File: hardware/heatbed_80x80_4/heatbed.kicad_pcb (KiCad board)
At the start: 2 copper layers, 80 x 80 mm, 1 part, among them J1 PWR

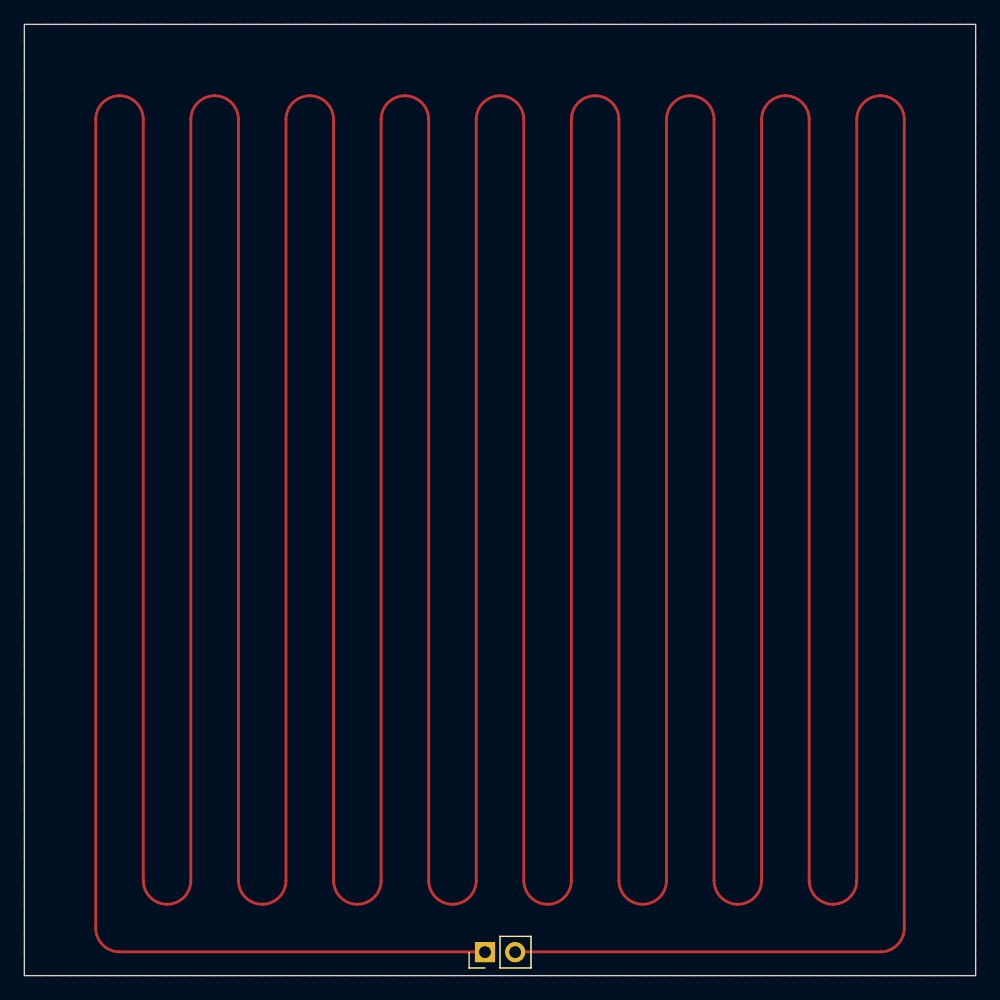
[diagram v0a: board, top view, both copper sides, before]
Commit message: Further increase tracks' widths
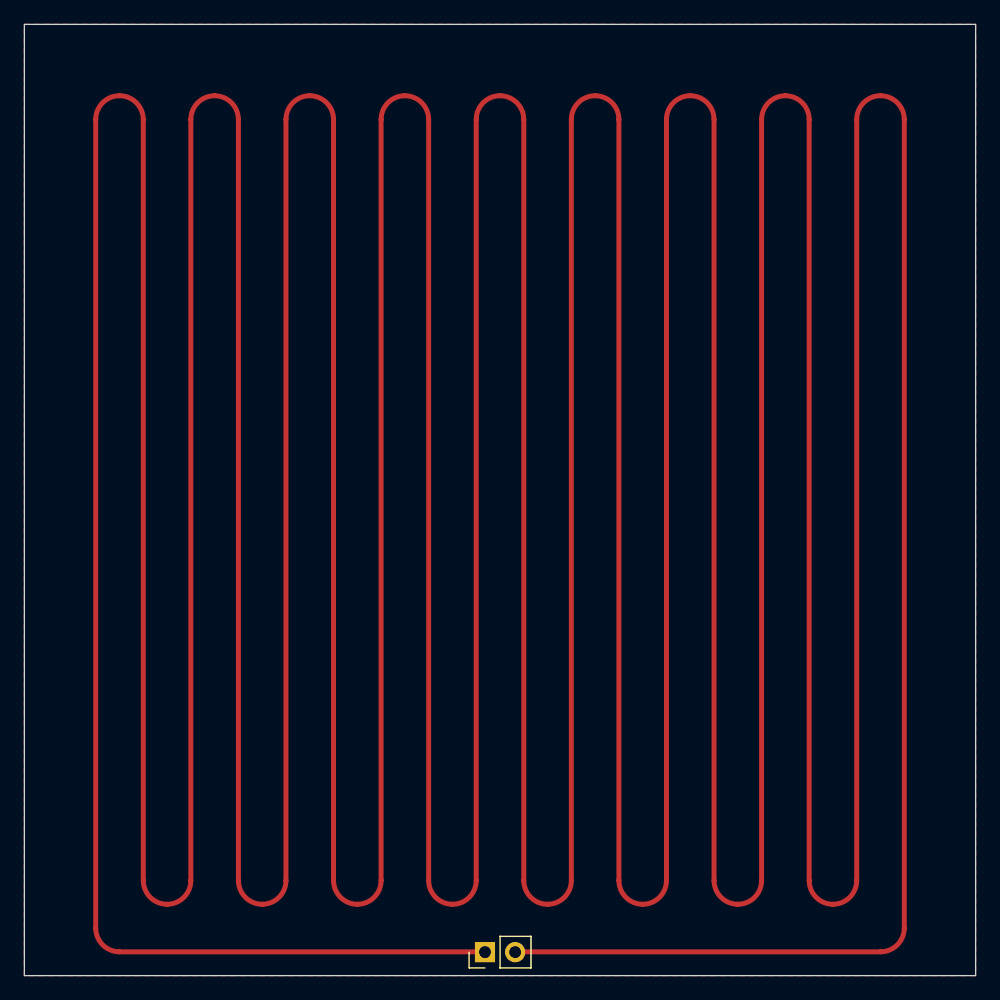
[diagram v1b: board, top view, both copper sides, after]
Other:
- board text added: "Width: 0.418 mm | Length: 1334.63 mm | Resistance: 2.91 Ω"
- board text removed: "Width: 0.241 mm | Length: 1334.63 mm | Resistance: 4.53 Ω"

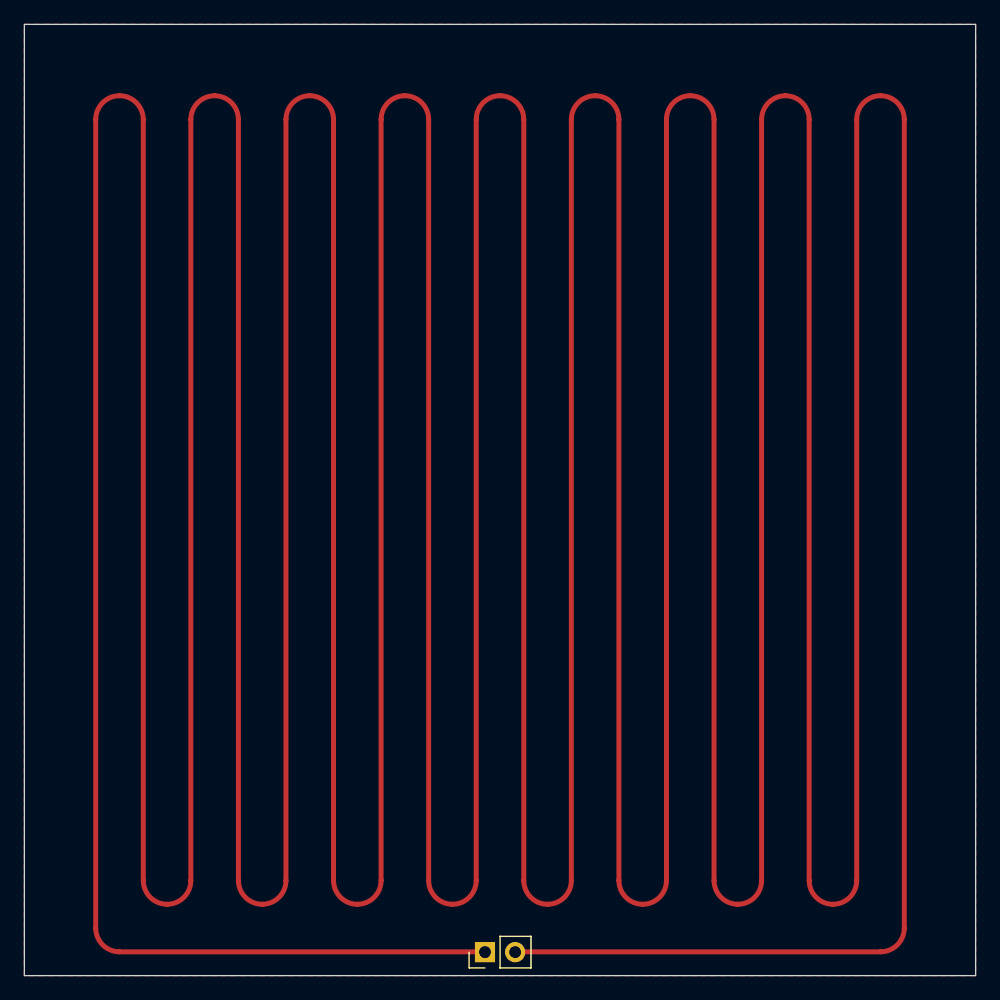
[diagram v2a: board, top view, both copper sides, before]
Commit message: Increase holes' diameters
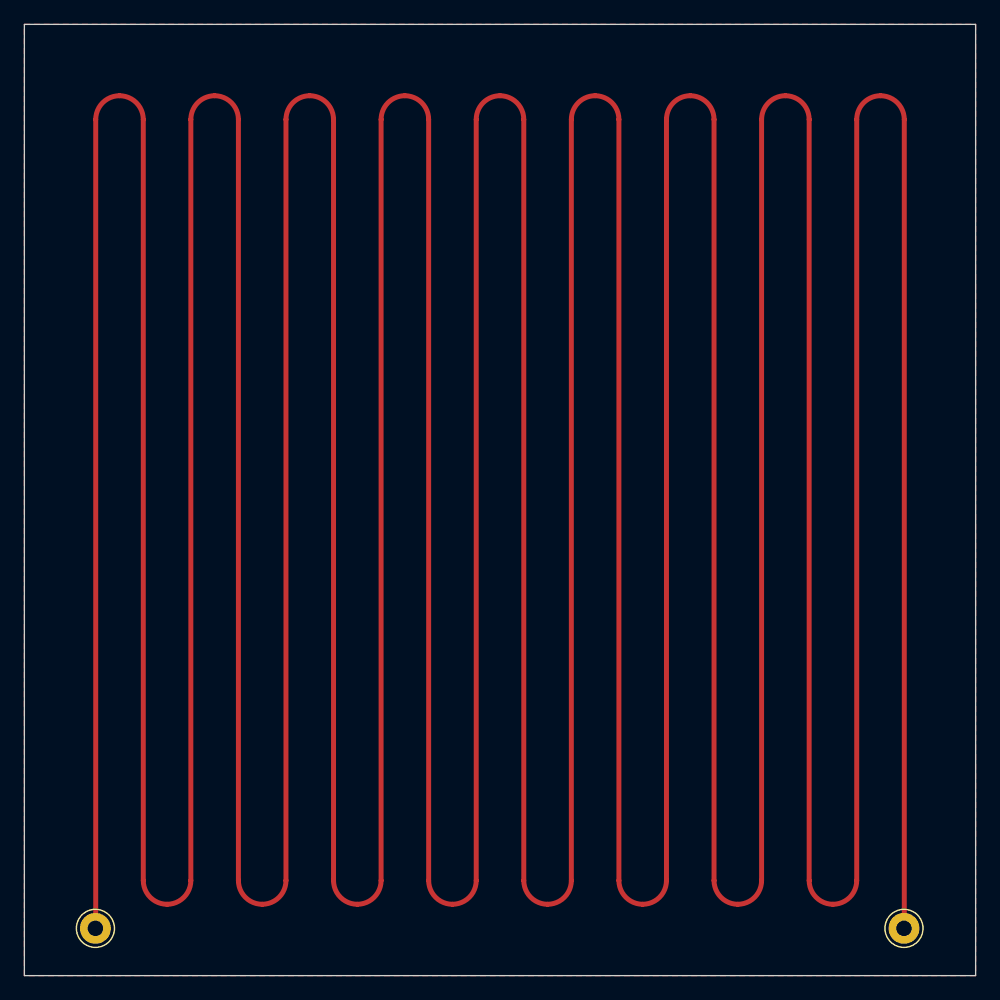
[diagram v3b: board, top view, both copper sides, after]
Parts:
- added J2: Conn_01x01, Connector_Pin:Pin_D1.3mm_L11.0mm, F.Cu at (181.0, 144.0)
- J1: value PWR -> Conn_01x01; footprint Connector_PinHeader_2.54mm:PinHeader_1x02_P2.54mm_Vertical -> Connector_Pin:Pin_D1.3mm_L11.0mm
- moved J1 32.8 mm to (113.0, 144.0), turned to 0 degrees
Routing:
- net Net-(J1-Pin_1): track 1331.7 -> 1264.2 mm
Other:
- board text removed: "Width: 0.418 mm | Length: 1334.63 mm | Resistance: 2.91 Ω"
